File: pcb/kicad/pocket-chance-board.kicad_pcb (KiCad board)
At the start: 4 copper layers, 150 x 100 mm, 150 parts, among them J1 SWD, J2 USB4085-GF-A, J3 LiPo JST-PH 2.0mm (1 = + RED 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, J4 LCD 1.54in ST7789 module, JST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, J5 Speaker JST-PH, J6 microSD Molex 104031-0811, J7 STEMMA QT, J8 Expansion (6 = VBAT_SENSE ADC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, J9 LCD header 2.54 mm (wire by n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, Q1 FS8205A, Q3 AO3400A, Q4 AO3401A, Q6 AO3401A (DNP: fit only for a 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, SW1 BOOT, SW10 DPAD LEFT PTS645SM43SMTR92, SW11 DPAD RIGHT PTS645SM43SMTR92, SW12 DPAD PRESS PTS645SM43SMTR92, SW2 RESET, SW3 POWER PCM12, SW4 A PTS125SM43SMTR2LFS, SW5 B PTS125SM43SMTR2LFS, SW6 X PTS125SM43SMTR2LFS, SW7 Y PTS125SM43SMTR2LFS, SW8 DPAD UP PTS645SM43SMTR92, SW9 DPAD DOWN PTS645SM43SMTR92, U1 RP2350A, U10 LSM6DSOXTR, U11 RM2, U2 W25Q128JVSIQ, U3 APS6404L-3SQR-SN, U4 USBLC6-2SC6, U5 BQ24074RGTR, U6 TPS63001DRCR, U7 DW01A, U8 PAM8302AADCR, U9 DS3231MZ+, Y1 12MHz ABM8-272-T3

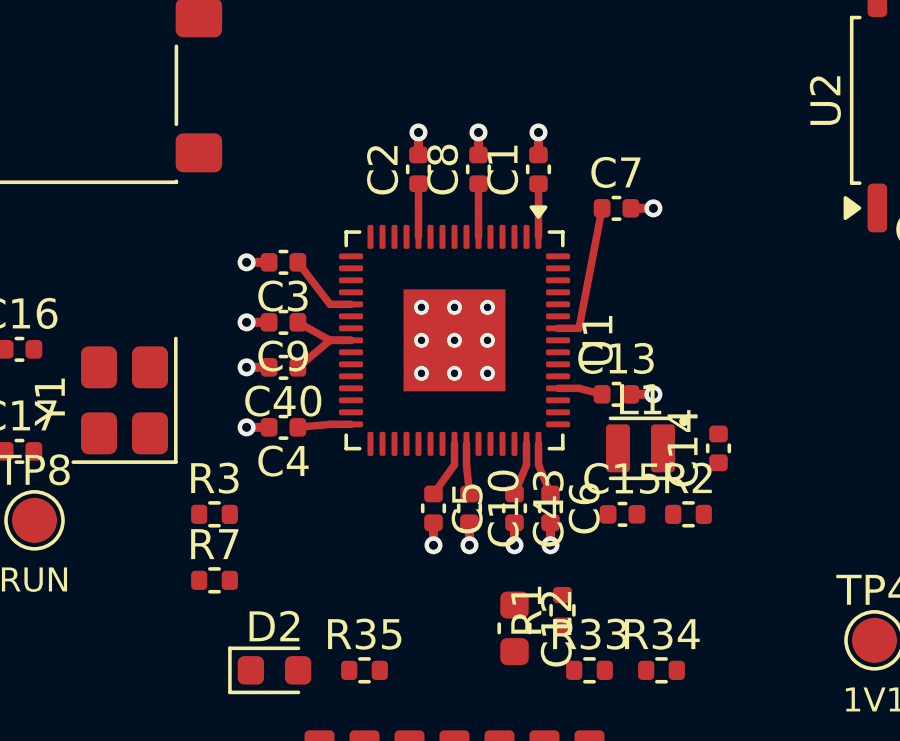
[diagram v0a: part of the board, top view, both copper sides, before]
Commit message: Routing stage 1 reworked: orthogonal escape stubs; C5/C10 shifted 0.3 mm; expert's rev 0.12 verification recorded; STAGE2 handoff
DRC: only the 382 unrouted connections. Schematic unchanged (rev 0.12, hash 51fe1bd6).

Co-Authored-By: Claude Fable 5.1 <noreply@anthropic.com>
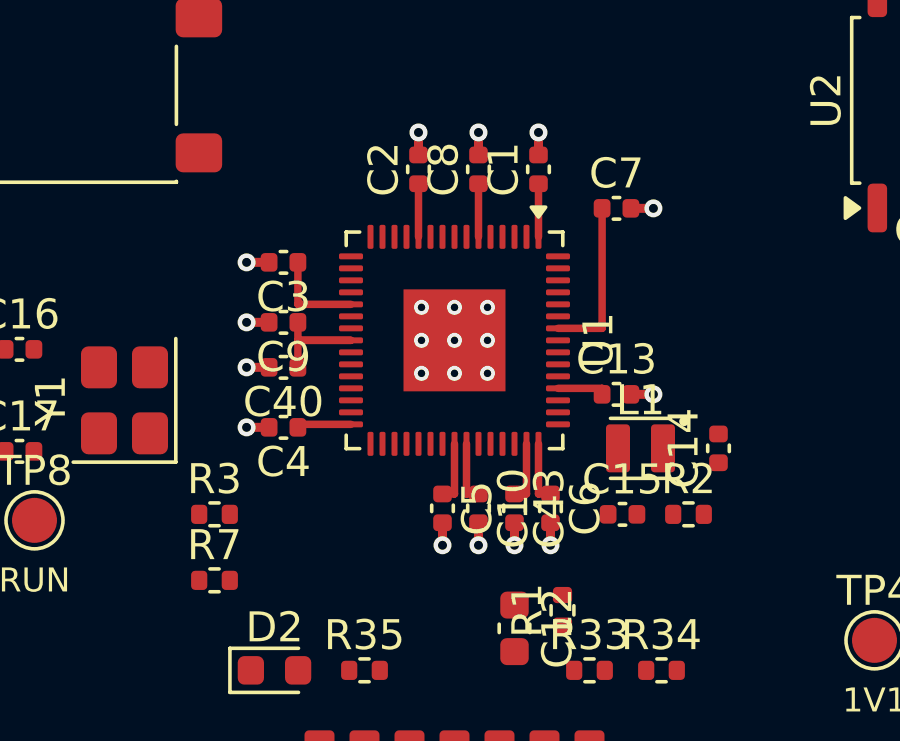
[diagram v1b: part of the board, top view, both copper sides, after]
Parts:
- moved C10 0.30 mm to (122.8, 125.6)
- moved C5 0.30 mm to (121.6, 125.6)
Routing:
- net +3V3: track 17.7 -> 19.9 mm
- net 1V1: track 7.47 -> 8.88 mm

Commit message: Rev 0.13 (John's yes): C44 1 uF 0603 at PSRAM VDD pin 8 (APS6404L-3SQR section 14.3); J-SD row corrected to push-pull
Netlist diff vs rev 0.12 (8e8ce9e): C44 added on +3V3/GND, nothing else. ERC 0 errors, 2 expected
warnings. Placed at (93.5, 56.6) beside U3 pin 8; DRC only unrouted connections.

Co-Authored-By: Claude Opus 5.5 <noreply@anthropic.com>
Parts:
- added C44: 1uF, Capacitor_SMD:C_0603_1608Metric, F.Cu at (143.5, 106.6)
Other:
- board text added: "Pocket Chance spin 1 rev 0.13 layout in progress"
- board text removed: "Pocket Chance spin 1 rev 0.12 layout in progress"

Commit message: Layout: C19 (100 nF) nearest PSRAM pin 8 at 3.0 mm, C44 (1 uF) behind it (expert, rev 0.13 review)
Co-Authored-By: Claude Opus 5.5 <noreply@anthropic.com>
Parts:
- moved C19 11.0 mm to (143.2, 106.9)
- moved C44 2.00 mm to (143.6, 104.6)
